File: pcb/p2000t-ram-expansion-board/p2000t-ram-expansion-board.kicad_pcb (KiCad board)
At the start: 2 copper layers, 11 parts, among them J1 EXTENSION BOARD, U1 74HC04, U10 74HC32, U2 CY62256-70PC, U3 74HC32, U4 CY62256-70PC, U5 74HC688, U6 74HC04, U7 74HC08, U8 74HC173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

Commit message: Revising design
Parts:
- removed the U1 at (80.8, 87.1)
- removed U10: 74HC32, Package_DIP:DIP-14_W7.62mm_Socket
- removed the U3 at (70.8, 62.1)
- removed the U7 at (80.8, 75.4)
- removed U9: 74HC08, Package_DIP:DIP-14_W7.62mm_Socket
- added C1: 0.1uF, Capacitor_THT:C_Disc_D5.0mm_W2.5mm_P5.00mm, F.Cu at (50.8, 64.8)
- added C2: 0.1uF, Capacitor_THT:C_Disc_D5.0mm_W2.5mm_P5.00mm, F.Cu at (31.7, 34.3)
- added C3: 0.1uF, Capacitor_THT:C_Disc_D5.0mm_W2.5mm_P5.00mm, F.Cu at (31.7, 64.8)
- added C4: 220uF, Capacitor_THT:CP_Radial_D6.3mm_P2.50mm, F.Cu at (152.4, 36.8)
- added C5: 0.1uF, Capacitor_THT:C_Disc_D5.0mm_W2.5mm_P5.00mm, F.Cu at (50.8, 34.3)
- added C6: 0.1uF, Capacitor_THT:C_Disc_D5.0mm_W2.5mm_P5.00mm, F.Cu at (139.7, 26.7)
- added C7: 0.1uF, Capacitor_THT:C_Disc_D5.0mm_W2.5mm_P5.00mm, F.Cu at (114.3, 26.7)
- added C8: 0.1uF, Capacitor_THT:C_Disc_D5.0mm_W2.5mm_P5.00mm, F.Cu at (88.9, 31.8)
- added C9: 0.1uF, Capacitor_THT:C_Disc_D5.0mm_W2.5mm_P5.00mm, F.Cu at (69.8, 36.8)
- added J2: POWER, Connector_PinHeader_2.54mm:PinHeader_1x02_P2.54mm_Vertical, F.Cu at (153.7, 24.1)
- added U2: 74HC00, Package_DIP:DIP-14_W7.62mm_Socket, F.Cu at (63.5, 41.9)
- added U5: 74HC00, Package_DIP:DIP-14_W7.62mm_Socket, F.Cu at (25.4, 69.8)
- added U8: 74LHC157, Package_DIP:DIP-16_W7.62mm_Socket, F.Cu at (25.4, 39.4)
- J1: value EXTENSION BOARD -> EXPANSION BOARD; footprint Connector_PinSocket_2.54mm:PinSocket_2x20_P2.54mm_Horizontal -> Connector_PinHeader_2.54mm:PinHeader_2x20_P2.54mm_Horizontal
- U6: value 74HC04 -> 74HC32
- moved U1 99.0 mm to (129.5, 31.8), turned to 0 degrees
- moved U3 90.8 mm to (104.2, 31.8), turned to 0 degrees
- moved J1 78.9 mm to (118.1, 76.6), turned to -90 degrees
- moved U7 69.9 mm to (44.1, 39.4), turned to 0 degrees
- moved U4 46.4 mm to (82.6, 36.8), turned to 0 degrees
- moved U6 27.1 mm to (44.5, 69.8), turned to 0 degrees
- renumbered U2 to U1, U4 to U3, U5 to U4, U8 to U7
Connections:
- J1 pad 10: D7 -> D6
- J1 pad 11: A0 -> A1
- J1 pad 12: A1 -> A0
- J1 pad 13: A2 -> A3
- J1 pad 14: A3 -> A2
- J1 pad 15: A4 -> A5
- J1 pad 16: A5 -> A4
- J1 pad 17: A6 -> A7
- J1 pad 18: A7 -> A6
- J1 pad 19: A8 -> A9
- J1 pad 2: unconnected-(J1-Pad2) -> GND
- J1 pad 20: A9 -> A8
- J1 pad 21: A10 -> A11
- J1 pad 22: A11 -> A10
- J1 pad 23: A12 -> A13
- J1 pad 24: A13 -> A12
- J1 pad 25: A14 -> RAMS2
- J1 pad 26: RAMS2 -> A14
- J1 pad 27: ~{MRQ} -> ~{RD}
- J1 pad 28: ~{RD} -> ~{MRQ}
- J1 pad 29: unconnected-(J1-Pad29) -> ~{WR}
- J1 pad 3: D0 -> D1
- J1 pad 30: ~{WR} -> unconnected-(J1-Pad30)
- J1 pad 31: ~{IORQ} -> unconnected-(J1-Pad31)
- J1 pad 32: unconnected-(J1-Pad32) -> ~{IORQ}
- J1 pad 33: unconnected-(J1-Pad33) -> ~{RES}
- J1 pad 34: ~{RES} -> unconnected-(J1-Pad34)
- J1 pad 4: D1 -> D0
- J1 pad 5: D2 -> D3
- J1 pad 6: D3 -> D2
- J1 pad 7: D4 -> D5
- J1 pad 8: D5 -> D4
- J1 pad 9: D6 -> D7
- U1 pad 1: A14P -> A14_1
- U1 pad 20: Net-(U2-Pad20) -> ~{CS1}
- U1 pad 26: A13P -> A13_1
- U3 pad 1: A14P -> A14_2
- U3 pad 20: Net-(U3-Pad8) -> ~{CS2}
- U3 pad 26: A13P -> A13_2
- U6 pad 1: (no net) -> Net-(U5-Pad3)
- U6 pad 10: (no net) -> S2
- U6 pad 11: (no net) -> ~{CS1}
- U6 pad 12: (no net) -> Net-(U5-Pad11)
- U6 pad 13: (no net) -> ~{REN}
- U6 pad 2: (no net) -> ~{REN}
- U6 pad 3: (no net) -> ~{CS2}
- U6 pad 4: (no net) -> Net-(U5-Pad6)
- U6 pad 5: (no net) -> Net-(U5-Pad8)
- U6 pad 6: (no net) -> Net-(U5-Pad12)
- U6 pad 8: (no net) -> Net-(U6-Pad8)
- U6 pad 9: (no net) -> S1
- U7 pad 11: GND -> D3
- U7 pad 15: Net-(U1-Pad12) -> RES
- U7 pad 7: Net-(U8-Pad7) -> WR
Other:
- board outline added: 140 x 70 mm
- board text added: "P2000T RAM EXPANSION BOARD 64kb (0-5 bank switching)"

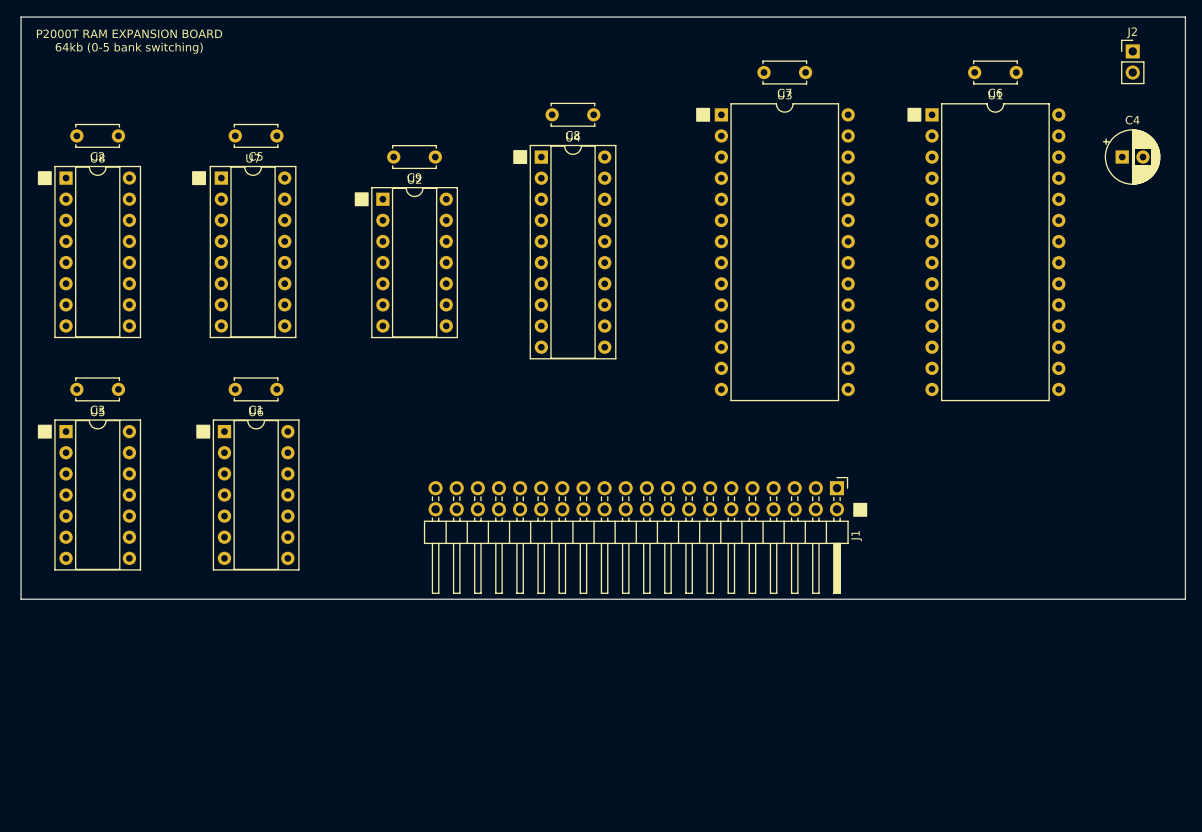
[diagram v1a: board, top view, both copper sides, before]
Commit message: Adding reverse polarity diode and silk screen comments
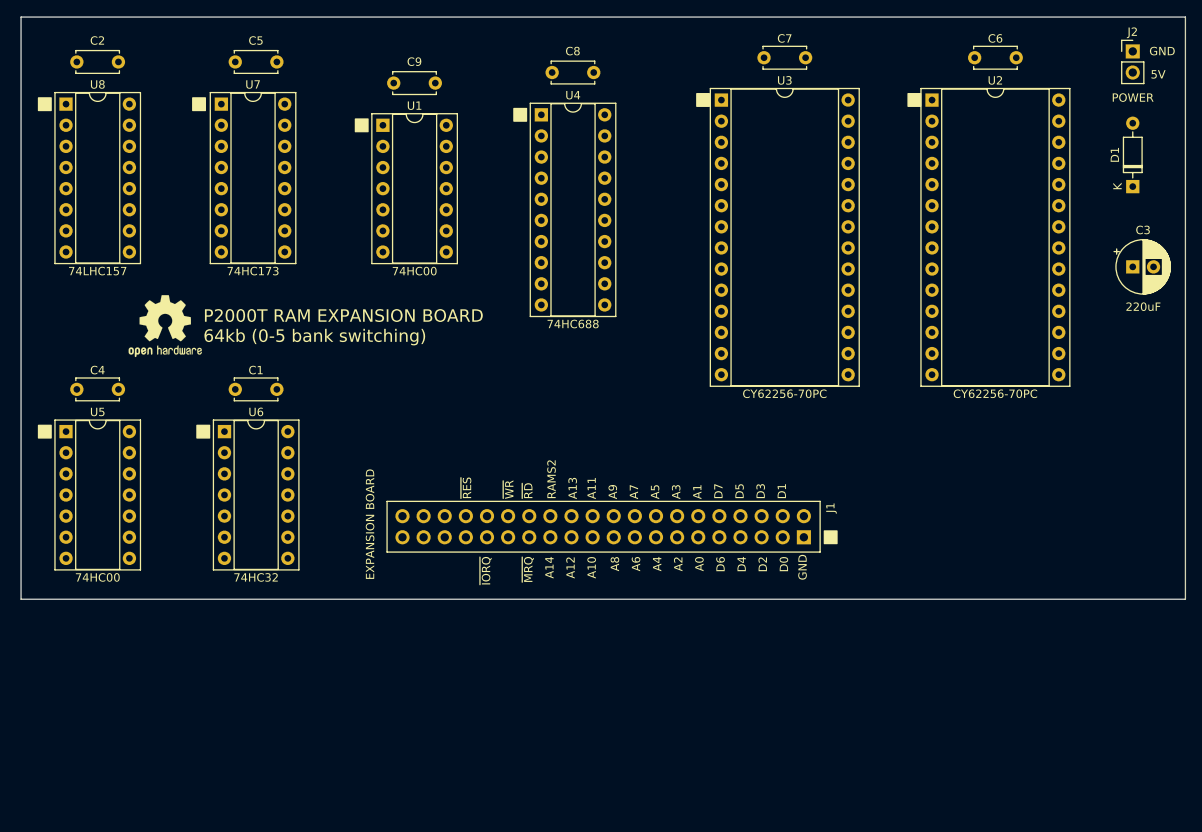
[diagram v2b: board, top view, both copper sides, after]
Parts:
- added D1: DIODE, Diode_THT:D_DO-35_SOD27_P7.62mm_Horizontal, F.Cu at (153.7, 40.4)
- added REF**: OSHW-Logo2_9.8x8mm_SilkScreen, Symbol:OSHW-Logo2_9.8x8mm_SilkScreen, F.Cu at (37.3, 57.1)
- J1: footprint Connector_PinHeader_2.54mm:PinHeader_2x20_P2.54mm_Horizontal -> Connector_PinHeader_2.54mm:PinHeader_2x20_P2.54mm_Vertical; moved to B.Cu
- U2: renamed from U1; footprint Package_DIP:DIP-28_W15.24mm -> Package_DIP:DIP-28_W15.24mm_Socket
- U3: footprint Package_DIP:DIP-28_W15.24mm -> Package_DIP:DIP-28_W15.24mm_Socket
- moved C3 13.3 mm to (153.7, 50.0)
- moved C2 8.89 mm to (31.7, 25.4)
- moved C5 8.89 mm to (50.8, 25.4)
- moved U1 8.89 mm to (63.5, 33.0)
- moved U7 8.89 mm to (44.1, 30.5)
- moved U8 8.89 mm to (25.4, 30.5)
- moved C9 8.89 mm to (69.8, 27.9)
- moved J1 7.12 mm to (114.1, 82.5), turned to 90 degrees
- moved U4 5.08 mm to (82.6, 31.8)
- moved C8 5.08 mm to (88.9, 26.7)
- moved C6 1.78 mm to (139.7, 24.9)
- moved C7 1.78 mm to (114.3, 24.9)
- moved U2 1.78 mm to (129.5, 30.0)
- moved U3 1.78 mm to (104.2, 30.0)
- renumbered C4 to C3, C3 to C4, U2 to U1
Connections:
- J1 pad 1: unconnected-(J1-Pad1) -> GND
- J1 pad 10: D6 -> D7
- J1 pad 11: A1 -> A0
- J1 pad 12: A0 -> A1
- J1 pad 13: A3 -> A2
- J1 pad 14: A2 -> A3
- J1 pad 15: A5 -> A4
- J1 pad 16: A4 -> A5
- J1 pad 17: A7 -> A6
- J1 pad 18: A6 -> A7
- J1 pad 19: A9 -> A8
- J1 pad 2: GND -> unconnected-(J1-Pad2)
- J1 pad 20: A8 -> A9
- J1 pad 21: A11 -> A10
- J1 pad 22: A10 -> A11
- J1 pad 23: A13 -> A12
- J1 pad 24: A12 -> A13
- J1 pad 25: RAMS2 -> A14
- J1 pad 26: A14 -> RAMS2
- J1 pad 27: ~{RD} -> ~{MRQ}
- J1 pad 28: ~{MRQ} -> ~{RD}
- J1 pad 29: ~{WR} -> unconnected-(J1-Pad29)
- J1 pad 3: D1 -> D0
- J1 pad 30: unconnected-(J1-Pad30) -> ~{WR}
- J1 pad 31: unconnected-(J1-Pad31) -> ~{IORQ}
- J1 pad 32: ~{IORQ} -> unconnected-(J1-Pad32)
- J1 pad 33: ~{RES} -> unconnected-(J1-Pad33)
- J1 pad 34: unconnected-(J1-Pad34) -> ~{RES}
- J1 pad 4: D0 -> D1
- J1 pad 5: D3 -> D2
- J1 pad 6: D2 -> D3
- J1 pad 7: D5 -> D4
- J1 pad 8: D4 -> D5
- J1 pad 9: D7 -> D6
- J2 pad 2: +5V -> Net-(J2-Pad2)
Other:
- board text added: "5V"
- board text added: "A0"
- board text added: "A1"
- board text added: "A10"
- board text added: "A11"
- board text added: "A12"
- board text added: "A13"
- board text added: "A14"
- board text added: "A2"
- board text added: "A3"
- board text added: "A4"
- board text added: "A5"
- board text added: "A6"
- board text added: "A7"
- board text added: "A8"
- board text added: "A9"
- board text added: "D0"
- board text added: "D1"
- board text added: "D2"
- board text added: "D3"
- board text added: "D4"
- board text added: "D5"
- board text added: "D6"
- board text added: "D7"
- board text added: "GND"
- board text added: "RAMS2"
- board text added: "~{IORQ}"
- board text added: "~{MRQ}"
- board text added: "~{RD}"
- board text added: "~{RES}"
- board text added: "~{WR}"

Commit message: Improving layout
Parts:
- U1: value 74HC00 -> 74HC04
- moved J1 2.03 mm to (114.1, 80.5)
- moved D1 0.25 mm to (153.7, 40.6)
- renumbered U5 to U3, U3 to U4, U4 to U5
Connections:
- net Net-(J2-Pad2) renamed VCC
- U1 pad 10: ~{MRQ} -> Net-(U1-Pad10)
- U1 pad 11: ~{REN} -> Net-(U1-Pad11)
- U1 pad 13: RAMS2 -> ~{MRQ}
- U1 pad 2: ~{RES} -> RES
- U1 pad 3: RES -> ~{WR}
- U1 pad 4: ~{WR} -> WR
- U1 pad 5: ~{WR} -> Net-(U1-Pad5)
- U1 pad 6: WR -> BR
- U1 pad 8: Net-(U1-Pad12) -> unconnected-(U1-Pad8)
- U1 pad 9: ~{MRQ} -> GND
- U3 pad 1: Net-(U5-Pad1) -> S1 | S2
- U3 pad 11: Net-(U5-Pad11) -> ~{REN}
- U3 pad 12: Net-(U5-Pad12) -> Net-(U1-Pad12)
- U3 pad 13: Net-(U5-Pad12) -> RAMS2
- U3 pad 2: A14 -> BR
- U3 pad 3: Net-(U5-Pad3) -> Net-(U1-Pad11)
- U3 pad 4: Net-(U5-Pad1) -> BR
- U3 pad 5: Net-(U5-Pad1) -> S1 | S2
- U3 pad 6: Net-(U5-Pad6) -> Net-(U3-Pad6)
- U3 pad 8: Net-(U5-Pad8) -> Net-(U1-Pad5)
- U3 pad 9: A14 -> A13
- U6 pad 1: Net-(U5-Pad3) -> Net-(U3-Pad6)
- U6 pad 12: Net-(U5-Pad11) -> Net-(U1-Pad10)
- U6 pad 4: Net-(U5-Pad6) -> GND
- U6 pad 5: Net-(U5-Pad8) -> GND
- U6 pad 6: Net-(U5-Pad12) -> unconnected-(U6-Pad6)
- U6 pad 8: Net-(U5-Pad1) -> S1 | S2
- U8 pad 1: A14 -> BR
- U8 pad 2: A13 -> A14
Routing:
- net GND: track 0.00 -> 709.7 mm, vias 0 -> 5
- net +5V: track 0.00 -> 348.5 mm, vias 0 -> 4
- net ~{WR}: track 0.00 -> 147.2 mm
- net D2: track 0.00 -> 144.1 mm, vias 0 -> 1
- net A13_1: track 0.00 -> 135.6 mm
- net A14_1: track 0.00 -> 126.4 mm
- net D0: track 0.00 -> 121.6 mm
- net D3: track 0.00 -> 119.8 mm, vias 0 -> 1
- net D1: track 0.00 -> 114.7 mm
- net ~{CS1}: track 0.00 -> 111.3 mm
- net A8: track 0.00 -> 108.3 mm
- net ~{RD}: track 0.00 -> 108.1 mm
- net A9: track 0.00 -> 107.1 mm
- net A2: track 0.00 -> 105.0 mm, vias 0 -> 1
- net BR: track 0.00 -> 104.9 mm
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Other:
- board text added: "9.6mm (socket)"

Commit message: Adding GERBERS
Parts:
- added J3: TERMINAL, TerminalBlock:TerminalBlock_bornier-2_P5.08mm, F.Cu at (26.5, 26.2)
- moved C3 131.7 mm to (25.4, 80.0)
- moved J2 128.1 mm to (26.5, 39.4)
- moved D1 127.9 mm to (26.5, 54.6)
- moved C7 94.4 mm to (26.7, 59.9), turned to -90 degrees
- moved REF** 85.2 mm to (120.7, 74.9), turned to 90 degrees
- moved U3 84.6 mm to (101.6, 33.0)
- moved C4 84.6 mm to (107.9, 27.9)
- moved U4 82.8 mm to (31.8, 70.0), turned to 90 degrees
- moved C6 75.8 mm to (72.4, 59.7), turned to -90 degrees
- moved U2 65.6 mm to (77.5, 69.9), turned to 90 degrees
- moved C1 54.9 mm to (91.4, 27.9)
- moved U6 54.8 mm to (85.1, 33.0)
- moved C8 35.6 mm to (124.4, 27.9)
- moved U5 35.6 mm to (118.1, 33.0)
- moved J1 15.1 mm to (99.1, 80.5)
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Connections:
- U1 pad 11: Net-(U1-Pad11) -> BR
- U1 pad 6: BR -> Net-(U1-Pad6)
- U3 pad 1: S1 | S2 -> Net-(U3-Pad1)
- U3 pad 2: BR -> Net-(U1-Pad6)
- U3 pad 3: Net-(U1-Pad11) -> BR
- U3 pad 4: BR -> GND
- U3 pad 5: S1 | S2 -> GND
- U3 pad 6: Net-(U3-Pad6) -> unconnected-(U3-Pad6)
- U6 pad 1: Net-(U3-Pad6) -> BR
- U6 pad 8: S1 | S2 -> Net-(U3-Pad1)
- U8 pad 2: A14 -> GND
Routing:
- net GND: track 709.7 -> 577.6 mm, vias 5 -> 0
- net A13_2: track 100.9 -> 9.80 mm, vias 1 -> 0
- net A13_1: track 135.6 -> 56.0 mm, vias 0 -> 1
- net Net-(U1-Pad11): track 71.0 -> 0.00 mm, vias 1 -> 0
- net A14_1: track 126.4 -> 62.4 mm, vias 0 -> 1
- net A4: track 75.1 -> 138.9 mm, vias 1 -> 0
- net ~{CS1}: track 111.3 -> 49.0 mm
- net ~{WR}: track 147.2 -> 96.9 mm, vias 0 -> 1
- net D2: track 144.1 -> 99.5 mm
- net Net-(U1-Pad6): track 0.00 -> 44.3 mm
- net A14: track 103.8 -> 61.2 mm
- net D4: track 52.2 -> 94.4 mm
- net A14_2: track 76.4 -> 34.3 mm
- net A7: track 83.6 -> 124.4 mm
- net S1 | S2: track 40.5 -> 0.00 mm
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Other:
- board size 140 x 70 mm -> 110 x 68.1 mm
- board text added: "jlcjlcjlcjlc"
- board text added: "rev0"
- board text added: "~{CS1}"
- board text added: "~{CS2}"
- board text removed: "9.6mm (socket)"

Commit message: Revising PCB and updating code
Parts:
- added D2: LED, LED_SMD:LED_0805_2012Metric_Pad1.15x1.40mm_HandSolder, F.Cu at (123.4, 30.5)
- added D3: LED, LED_SMD:LED_0805_2012Metric_Pad1.15x1.40mm_HandSolder, F.Cu at (123.4, 34.0)
- added D4: LED, LED_SMD:LED_0805_2012Metric_Pad1.15x1.40mm_HandSolder, F.Cu at (123.4, 37.6)
- added R1: R, Resistor_SMD:R_0805_2012Metric_Pad1.20x1.40mm_HandSolder, F.Cu at (118.4, 30.5)
- added R2: R, Resistor_SMD:R_0805_2012Metric_Pad1.20x1.40mm_HandSolder, F.Cu at (118.4, 34.0)
- added R3: R, Resistor_SMD:R_0805_2012Metric_Pad1.20x1.40mm_HandSolder, F.Cu at (118.4, 37.6)
- U8: value 74LHC157 -> 74HC157
- moved U5 21.8 mm to (118.1, 54.9)
- moved C8 21.3 mm to (124.4, 49.3)
- moved REF** 11.6 mm to (110.0, 79.5), turned to 0 degrees
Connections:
- net WR renamed Net-(U1-Pad4)
- U1 pad 11: BR -> Net-(U1-Pad11)
- U1 pad 3: ~{WR} -> Net-(U1-Pad3)
- U1 pad 6: Net-(U1-Pad6) -> EO
- U3 pad 2: Net-(U1-Pad6) -> EO
- U3 pad 3: BR -> Net-(U1-Pad11)
- U5 pad 1: GND -> ~{IORQ}
- U6 pad 1: BR -> Net-(U1-Pad11)
- U6 pad 4: GND -> Net-(U5-Pad19)
- U6 pad 5: GND -> ~{WR}
- U6 pad 6: unconnected-(U6-Pad6) -> Net-(U1-Pad3)
- U7 pad 10: ~{IORQ} -> GND
- U7 pad 9: Net-(U5-Pad19) -> GND
- U8 pad 1: BR -> EO
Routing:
- net GND: track 577.6 -> 686.8 mm
- net EO: track 0.00 -> 90.8 mm
- net BR: track 77.8 -> 0.00 mm
- net S0: track 27.2 -> 98.0 mm
- net +5V: track 328.3 -> 372.8 mm
- net Net-(U1-Pad6): track 44.3 -> 0.00 mm
- net ~{IORQ}: track 37.3 -> 71.9 mm
- net A0: track 112.9 -> 80.0 mm
- net Net-(U1-Pad11): track 0.00 -> 32.6 mm, vias 0 -> 1
- net S2: track 59.2 -> 90.7 mm, vias 0 -> 1
- net S1: track 43.8 -> 75.1 mm
- net ~{CS1}: track 49.0 -> 17.9 mm
- net Net-(U1-Pad3): track 0.00 -> 27.3 mm, vias 0 -> 1
- net A1: track 106.7 -> 79.5 mm
- net D1: track 100.5 -> 126.6 mm, vias 1 -> 0
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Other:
- board text added: "(Can be left unpopulated)"
- board text added: "BANK SWITCHING LEDS"
- board text added: "S0"
- board text added: "S1"
- board text added: "S2"
- board text added: "rev1"
- board text removed: "rev0"

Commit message: Polishing PCB
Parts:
- moved REF** 1.92 mm to (109.7, 77.6)
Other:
- board text added: "100uF works as well"
- board text added: "Date"
- board text added: "OK?"
- board text added: "Resistor values depend on choice of LEDs"
- board text added: "www.philips-p2000t.nl"
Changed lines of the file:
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@@
       (effects (font (size 1 1) (thickness 0.15)))
     )
-    (fp_text value "0.1uF" (at 2.49 -2.54) (layer "F.Fab")
+    (fp_text value "0.1uF" (at 2.413 2.54) (layer "F.SilkS")
       (effects (font (size 1 1) (thickness 0.15)))
     )
@@
       (effects (font (size 1 1) (thickness 0.15)))
     )
-    (fp_text value "0.1uF" (at 2.5 2.5) (layer "F.Fab")
+    (fp_text value "0.1uF" (at 2.5 2.5) (layer "F.SilkS")
       (effects (font (size 1 1) (thickness 0.15)))
     )
@@
       (effects (font (size 1 1) (thickness 0.15)))
     )
-    (fp_text value "0.1uF" (at 2.5 2.5) (layer "F.Fab")
+    (fp_text value "0.1uF" (at 2.5 2.5) (layer "F.SilkS")
       (effects (font (size 1 1) (thickness 0.15)))
     )
@@
       (effects (font (size 1 1) (thickness 0.15)))
     )
-    (fp_text value "0.1uF" (at 2.5 2.5 -270) (layer "F.Fab")
+    (fp_text value "0.1uF" (at -2.072 0 -180) (layer "F.SilkS")
       (effects (font (size 1 1) (thickness 0.15)))
     )
@@
       (effects (font (size 1 1) (thickness 0.15)))
     )
-    (fp_text value "0.1uF" (at 2.5 2.5 -270) (layer "F.Fab")
+    (fp_text value "0.1uF" (at -1.956 0 -180) (layer "F.SilkS")
       (effects (font (size 1 1) (thickness 0.15)))
     )
@@
       (effects (font (size 1 1) (thickness 0.15)))
     )
-    (fp_text value "0.1uF" (at 2.49 -2.54) (layer "F.Fab")
+    (fp_text value "0.1uF" (at 2.5 2.413) (layer "F.SilkS")
       (effects (font (size 1 1) (thickness 0.15)))
     )
@@
       (effects (font (size 1 1) (thickness 0.15)))
     )
-    (fp_text value "0.1uF" (at 2.5 2.5) (layer "F.Fab")
+    (fp_text value "0.1uF" (at 2.5 2.5) (layer "F.SilkS")
       (effects (font (size 1 1) (thickness 0.15)))
     )
@@
     )
   )
-  (footprint "Symbol:OSHW-Logo2_9.8x8mm_SilkScreen" locked (layer "F.Cu")
-    (at 109.982 79.502)
+  (footprint "Symbol:OSHW-Logo2_9.8x8mm_SilkScreen" (layer "F.Cu")
+    (at 109.728 77.597)
     (descr "Open Source Hardware Symbol")
     (tags "Logo Symbol OSHW")
@@
     )
   )
+  (gr_rect (start 33.3375 65.024) (end 63.6905 59.944) (layer "B.SilkS") (width 0.15) (fill solid))
   (gr_rect (start 114.808 54.102) (end 116.332 55.626) (layer "F.SilkS") (width 0.15) (fill solid))
   (gr_rect (start 48.768 29.718) (end 50.292 31.242) (layer "F.SilkS") (width 0.15) (fill solid))
@@
   (gr_rect (start 65.278 32.258) (end 66.802 33.782) (layer "F.SilkS") (width 0.15) (fill solid))
   (gr_rect (start 98.298 32.258) (end 99.822 33.782) (layer "F.SilkS") (width 0.15) (fill solid))
+  (gr_rect (start 36.195 75.438) (end 41.275 80.518) (layer "F.SilkS") (width 0.15) (fill solid))
   (gr_rect (start 76.723 73.152) (end 78.247 71.628) (layer "F.SilkS") (width 0.15) (fill solid))
   (gr_rect (start 101.516 79.756) (end 103.04 81.28) (layer "F.SilkS") (width 0.15) (fill solid))
+  (gr_rect (start 36.195 81.661) (end 41.275 86.741) (layer "F.SilkS") (width 0.15) (fill solid))
   (gr_rect (start 30.988 73.406) (end 32.512 71.882) (layer "F.SilkS") (width 0.15) (fill solid))
+  (gr_line (start 102.997 84.074) (end 128.27 84.074) (layer "F.SilkS") (width 0.15))
   (gr_rect (start 48.938 76.2) (end 101.008 82.296) (layer "F.SilkS") (width 0.15) (fill none))
   (gr_line (start 74.93 90) (end 74.93 21.844) (layer "Dwgs.User") (width 0.15))
@@
   (gr_arc (start 21.336 89.9668) (mid 20.366132 89.565068) (end 19.9644 88.5952) (layer "Edge.Cuts") (width 0.1))
   (gr_line (start 128.5748 21.844) (end 21.336 21.844) (layer "Edge.Cuts") (width 0.1))
+  (gr_text "Date" (at 31.877 62.484 270) (layer "B.SilkS")
+    (effects (font (size 1.5 1.5) (thickness 0.2)) (justify mirror))
+  )
   (gr_text "~{RD}" (at 65.956 75.946 90) (layer "F.SilkS")
     (effects (font (size 1 1) (thickness 0.15)) (justify left))
@@
     (effects (font (size 1 1) (thickness 0.15)) (justify right))
   )
+  (gr_text "www.philips-p2000t.nl" (at 115.57 82.804) (layer "F.SilkS")
+    (effects (font (size 1.2 1.2) (thickness 0.15)))
+  )
   (gr_text "BANK SWITCHING\nLEDS" (at 114.3 41.148) (layer "F.SilkS")
     (effects (font (size 1 1) (thickness 0.15)) (justify left))
@@
     (effects (font (size 1 1) (thickness 0.15)))
   )
+  (gr_text "OK?" (at 42.672 77.851 90) (layer "F.SilkS")
+    (effects (font (size 1 1) (thickness 0.15)))
+  )
   (gr_text "A4" (at 81.45 82.804 90) (layer "F.SilkS")
     (effects (font (size 1 1) (thickness 0.15)) (justify right))
@@
     (effects (font (size 1 1) (thickness 0.15)))
   )
+  (gr_text "Resistor values\ndepend on choice\nof LEDs" (at 115.443 26.162) (layer "F.SilkS")
+    (effects (font (size 0.7 0.7) (thickness 0.1)) (justify left))
+  )
   (gr_text "A14" (at 68.496 82.804 90) (layer "F.SilkS")
     (effects (font (size 1 1) (thickness 0.15)) (justify right))
@@
     (effects (font (size 0.7 0.7) (thickness 0.1)))
   )
+  (gr_text "100uF\nworks\nas well" (at 32.258 80.01) (layer "F.SilkS")
+    (effects (font (size 0.7 0.7) (thickness 0.1)))
+  )

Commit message: Putting link to Github repo on PCB
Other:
- board text added: "https://github.com/ifilot/p2000t-ram-expansion-board"
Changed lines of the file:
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@@
     (effects (font (size 1.5 1.5) (thickness 0.2)) (justify mirror))
+  )
+  (gr_text "jlcjlcjlcjlc" (at 25.654 88.011) (layer "B.SilkS")
+    (effects (font (size 1 1) (thickness 0.15)) (justify mirror))
   )
   (gr_text "~{RD}" (at 65.956 75.946 90) (layer "F.SilkS")
@@
     (effects (font (size 1 1) (thickness 0.15)))
   )
+  (gr_text "https://github.com/ifilot/p2000t-ram-expansion-board" (at 128.397 57.404 90) (layer "F.SilkS")
+    (effects (font (size 1 1) (thickness 0.15)))
+  )
   (gr_text "A3" (at 83.736 75.946 90) (layer "F.SilkS")
     (effects (font (size 1 1) (thickness 0.15)) (justify left))
@@
     (effects (font (size 1 1) (thickness 0.15)) (justify left))
   )
-  (gr_text "jlcjlcjlcjlc" (at 25.4 87.63) (layer "F.SilkS")
-    (effects (font (size 1 1) (thickness 0.15)))
-  )
   (gr_text "D7" (at 88.816 75.946 90) (layer "F.SilkS")
